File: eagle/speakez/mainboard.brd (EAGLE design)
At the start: 42 parts, among them U1 +12v

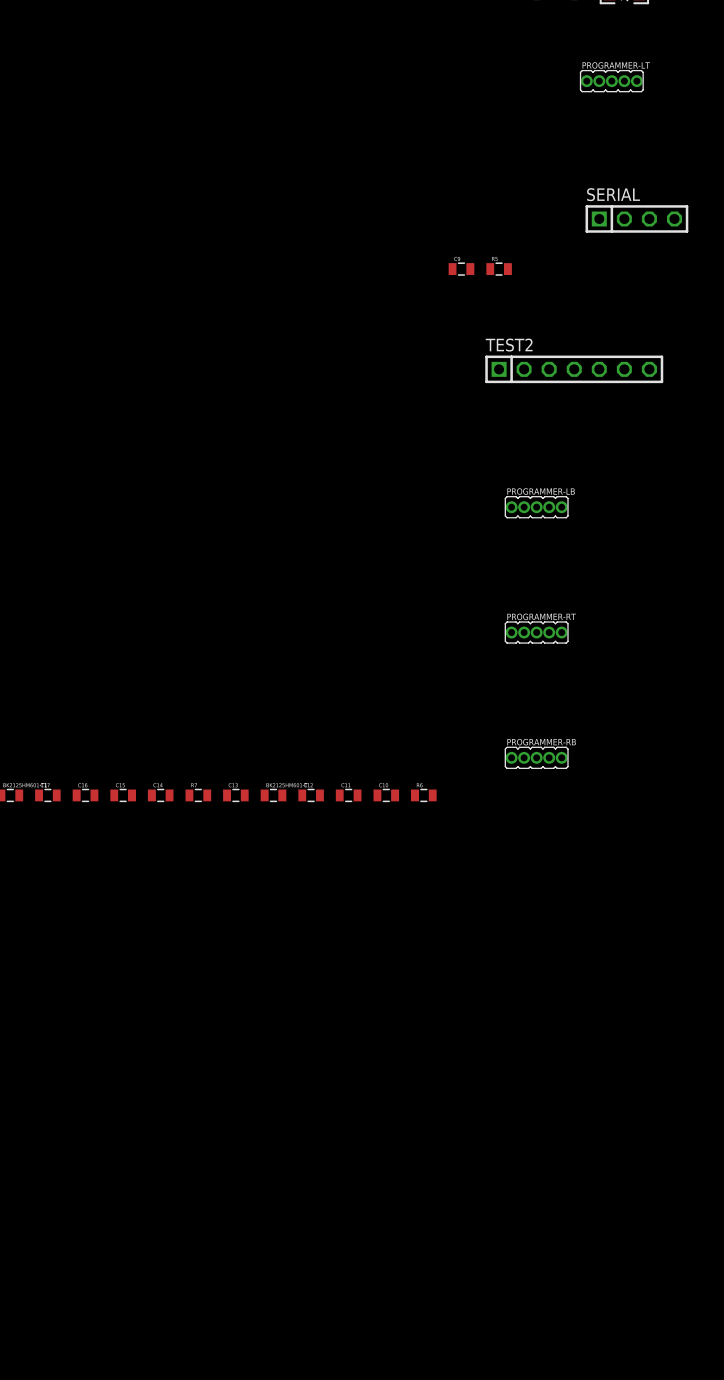
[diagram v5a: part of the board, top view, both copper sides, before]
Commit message: 0.05" header to 0.1" header
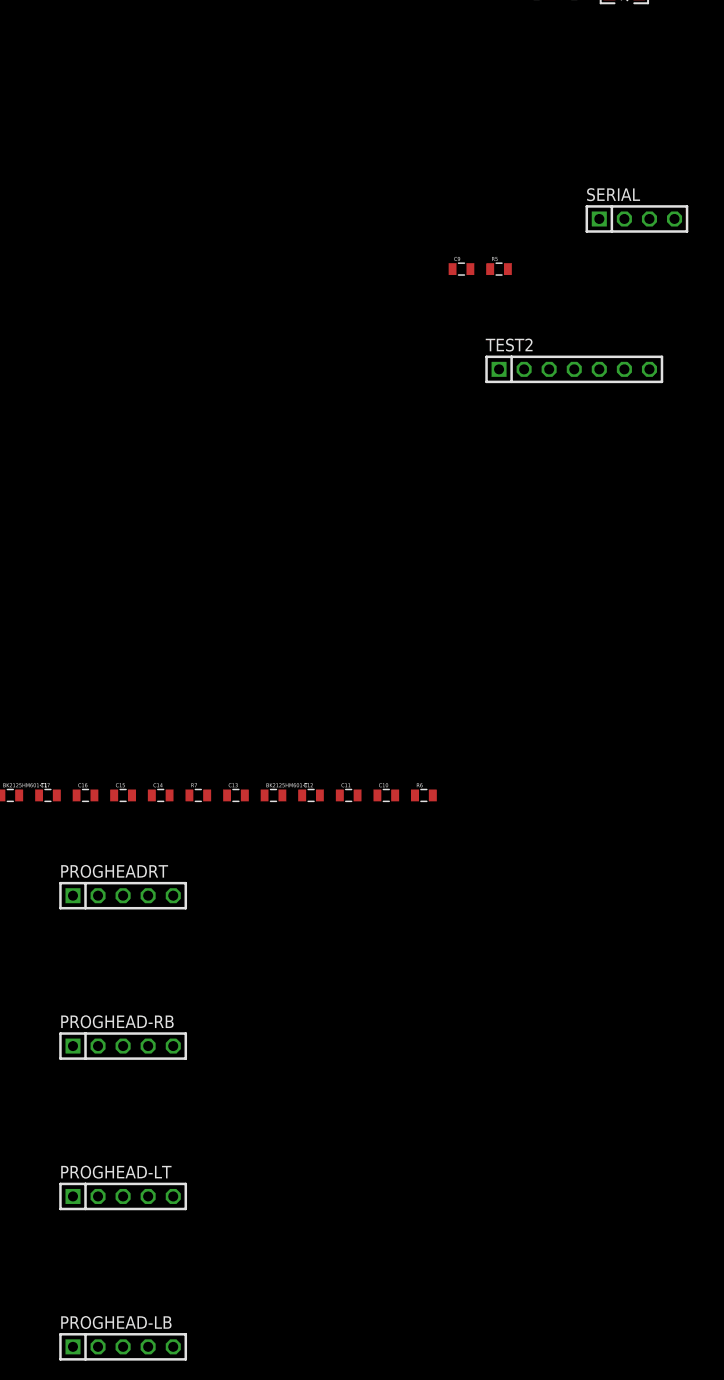
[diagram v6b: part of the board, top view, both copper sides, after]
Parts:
- removed PROGRAMMER-LB, PROGRAMMER-LT, PROGRAMMER-RB, PROGRAMMER-RT: PH1X5-05, pel_hdr:PH005-1-5
- added PROGHEAD-LB, PROGHEAD-LT, PROGHEAD-RB, PROGHEADRT: (no value), pinhead:1X05
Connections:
- net GND: now also PROGHEAD-RB.1, PROGHEAD-RB.2, PROGHEAD-RB.3, PROGHEAD-RB.4, PROGHEAD-RB.5, PROGHEADRT.2, PROGHEADRT.3, PROGHEADRT.4, PROGHEADRT.5; no longer PROGRAMMER-RB.1, PROGRAMMER-RB.2, PROGRAMMER-RB.3, PROGRAMMER-RB.4, PROGRAMMER-RB.5, PROGRAMMER-RT.2, PROGRAMMER-RT.3, PROGRAMMER-RT.4, PROGRAMMER-RT.5
- net N$14: now also PROGHEAD-LT.5; no longer PROGRAMMER-LT.5
- net N$20: now also PROGHEAD-LB.3; no longer PROGRAMMER-LB.3
- net N$21: now also PROGHEAD-LB.4; no longer PROGRAMMER-LB.4
- net N$23: now also PROGHEAD-LT.3; no longer PROGRAMMER-LT.3
- net N$24: now also PROGHEAD-LT.4; no longer PROGRAMMER-LT.4
- net N$3: now also PROGHEAD-LT.1; no longer PROGRAMMER-LT.1
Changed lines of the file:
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@@
 <element name="R3" library="SparkFun-Passives" package="0805" value="66 ohms" x="-57.15" y="-86.36"/>
 <element name="R4" library="SparkFun-Passives" package="0805" value="10k" x="-60.96" y="-86.36"/>
-<element name="PROGRAMMER-LT" library="pel_hdr" package="PH005-1-5" value="PH1X5-05" x="-55.88" y="-95.25"/>
 <element name="SERIAL" library="pinhead" package="1X04" value="" x="-50.8" y="-109.22"/>
 <element name="R5" library="SparkFun-Passives" package="0805" value="50k" x="-64.77" y="-114.3"/>
 <element name="C9" library="SparkFun-Capacitors" package="0805" value="" x="-68.58" y="-114.3"/>
 <element name="TEST2" library="pinhead" package="1X07" value="" x="-57.15" y="-124.46"/>
-<element name="PROGRAMMER-LB" library="pel_hdr" package="PH005-1-5" value="PH1X5-05" x="-63.5" y="-138.43"/>
-<element name="PROGRAMMER-RT" library="pel_hdr" package="PH005-1-5" value="PH1X5-05" x="-63.5" y="-151.13"/>
-<element name="PROGRAMMER-RB" library="pel_hdr" package="PH005-1-5" value="PH1X5-05" x="-63.5" y="-163.83"/>
 <element name="R6" library="SparkFun-Passives" package="0805" value="100k" x="-72.39" y="-167.64"/>
 <element name="C10" library="SparkFun-Capacitors" package="0805" value="0.1uF" x="-76.2" y="-167.64"/>
@@
 <element name="C17" library="SparkFun-Capacitors" package="0805" value="2.2uF" x="-110.49" y="-167.64"/>
 <element name="BK2125HM601-T1" library="SparkFun-Passives" package="0805" value="" x="-114.3" y="-167.64"/>
+<element name="PROGHEADRT" library="pinhead" package="1X05" value="" x="-102.87" y="-177.8"/>
+<element name="PROGHEAD-RB" library="pinhead" package="1X05" value="" x="-102.87" y="-193.04"/>
+<element name="PROGHEAD-LT" library="pinhead" package="1X05" value="" x="-102.87" y="-208.28"/>
+<element name="PROGHEAD-LB" library="pinhead" package="1X05" value="" x="-102.87" y="-223.52"/>
 </elements>
 <signals>
@@
 <contactref element="C11" pad="2"/>
 <contactref element="C12" pad="2"/>
-<contactref element="PROGRAMMER-RT" pad="2"/>
-<contactref element="PROGRAMMER-RT" pad="3"/>
-<contactref element="PROGRAMMER-RT" pad="4"/>
-<contactref element="PROGRAMMER-RT" pad="5"/>
-<contactref element="PROGRAMMER-RB" pad="1"/>
-<contactref element="PROGRAMMER-RB" pad="2"/>
-<contactref element="PROGRAMMER-RB" pad="3"/>
-<contactref element="PROGRAMMER-RB" pad="4"/>
-<contactref element="PROGRAMMER-RB" pad="5"/>
 <contactref element="BATTERY" pad="2"/>
 <contactref element="U1" pad="3"/>
@@
 <contactref element="C13" pad="2"/>
 <contactref element="BK2125HM601-T1" pad="2"/>
+<contactref element="PROGHEADRT" pad="2"/>
+<contactref element="PROGHEADRT" pad="3"/>
+<contactref element="PROGHEADRT" pad="4"/>
+<contactref element="PROGHEADRT" pad="5"/>
+<contactref element="PROGHEAD-RB" pad="1"/>
+<contactref element="PROGHEAD-RB" pad="2"/>
+<contactref element="PROGHEAD-RB" pad="3"/>
+<contactref element="PROGHEAD-RB" pad="4"/>
+<contactref element="PROGHEAD-RB" pad="5"/>
 <wire x1="-79.11" y1="-167.64" x2="-82.92" y2="-167.64" width="0" layer="19" extent="1-1"/>
 <wire x1="-75.3" y1="-167.64" x2="-79.11" y2="-167.64" width="0" layer="19" extent="1-1"/>
 <wire x1="-90.54" y1="-167.64" x2="-82.92" y2="-167.64" width="0" layer="19" extent="1-1"/>
 <wire x1="-98.16" y1="-167.64" x2="-90.54" y2="-167.64" width="0" layer="19" extent="1-1"/>
-<wire x1="-63.5" y1="-163.83" x2="-75.3" y2="-167.64" width="0" layer="19" extent="1-1"/>
-<wire x1="-62.23" y1="-163.83" x2="-63.5" y2="-163.83" width="0" layer="19" extent="1-1"/>
-<wire x1="-60.96" y1="-163.83" x2="-62.23" y2="-163.83" width="0" layer="19" extent="1-1"/>
-<wire x1="-59.69" y1="-163.83" x2="-60.96" y2="-163.83" width="0" layer="19" extent="1-1"/>
-<wire x1="-58.42" y1="-163.83" x2="-59.69" y2="-163.83" width="0" layer="19" extent="1-1"/>
-<wire x1="-62.23" y1="-151.13" x2="-62.23" y2="-163.83" width="0" layer="19" extent="1-1"/>
-<wire x1="-60.96" y1="-151.13" x2="-62.23" y2="-151.13" width="0" layer="19" extent="1-1"/>
-<wire x1="-59.69" y1="-151.13" x2="-60.96" y2="-151.13" width="0" layer="19" extent="1-1"/>
-<wire x1="-58.42" y1="-151.13" x2="-59.69" y2="-151.13" width="0" layer="19" extent="1-1"/>
-<wire x1="-113.4" y1="-167.64" x2="-98.16" y2="-167.64" width="0" layer="19" extent="1-1"/>
-<wire x1="-65.67" y1="-114.3" x2="-62.23" y2="-151.13" width="0" layer="19" extent="1-1"/>
+<wire x1="-97.79" y1="-177.8" x2="-98.16" y2="-167.64" width="0" layer="19" extent="1-1"/>
+<wire x1="-100.33" y1="-177.8" x2="-97.79" y2="-177.8" width="0" layer="19" extent="1-1"/>
+<wire x1="-102.87" y1="-177.8" x2="-100.33" y2="-177.8" width="0" layer="19" extent="1-1"/>
+<wire x1="-105.41" y1="-177.8" x2="-102.87" y2="-177.8" width="0" layer="19" extent="1-1"/>
+<wire x1="-113.4" y1="-167.64" x2="-105.41" y2="-177.8" width="0" layer="19" extent="1-1"/>
+<wire x1="-105.41" y1="-193.04" x2="-105.41" y2="-177.8" width="0" layer="19" extent="1-1"/>
+<wire x1="-107.95" y1="-193.04" x2="-105.41" y2="-193.04" width="0" layer="19" extent="1-1"/>
+<wire x1="-102.87" y1="-193.04" x2="-105.41" y2="-193.04" width="0" layer="19" extent="1-1"/>
+<wire x1="-100.33" y1="-193.04" x2="-102.87" y2="-193.04" width="0" layer="19" extent="1-1"/>
+<wire x1="-97.79" y1="-193.04" x2="-100.33" y2="-193.04" width="0" layer="19" extent="1-1"/>
+<wire x1="-65.67" y1="-114.3" x2="-75.3" y2="-167.64" width="0" layer="19" extent="1-1"/>
 <wire x1="-46.99" y1="-109.22" x2="-65.67" y2="-114.3" width="0" layer="19" extent="1-1"/>
 <wire x1="-58.05" y1="-86.36" x2="-46.99" y2="-109.22" width="0" layer="19" extent="1-1"/>
@@
 <contactref element="SERIAL" pad="3"/>
 <contactref element="TEST2" pad="1"/>
-<contactref element="PROGRAMMER-LT" pad="1"/>
 <contactref element="R6" pad="1"/>
 <contactref element="C10" pad="1"/>
@@
 <contactref element="TEST2" pad="6"/>
 <contactref element="TEST2" pad="7"/>
+<contactref element="PROGHEAD-LT" pad="1"/>
 <wire x1="-80.91" y1="-167.64" x2="-84.72" y2="-167.64" width="0" layer="19" extent="1-1"/>
 <wire x1="-77.1" y1="-167.64" x2="-80.91" y2="-167.64" width="0" layer="19" extent="1-1"/>
@@
 <wire x1="-92.34" y1="-167.64" x2="-88.53" y2="-167.64" width="0" layer="19" extent="1-1"/>
 <wire x1="-99.96" y1="-167.64" x2="-92.34" y2="-167.64" width="0" layer="19" extent="1-1"/>
+<wire x1="-107.95" y1="-208.28" x2="-99.96" y2="-167.64" width="0" layer="19" extent="1-1"/>
 <wire x1="-64.77" y1="-124.46" x2="-73.29" y2="-167.64" width="0" layer="19" extent="1-1"/>
 <wire x1="-52.07" y1="-124.46" x2="-64.77" y2="-124.46" width="0" layer="19" extent="1-1"/>
 <wire x1="-49.53" y1="-124.46" x2="-52.07" y2="-124.46" width="0" layer="19" extent="1-1"/>
 <wire x1="-49.53" y1="-109.22" x2="-49.53" y2="-124.46" width="0" layer="19" extent="1-1"/>
-<wire x1="-55.88" y1="-95.25" x2="-49.53" y2="-109.22" width="0" layer="19" extent="1-1"/>
-<wire x1="-61.86" y1="-86.36" x2="-55.88" y2="-95.25" width="0" layer="19" extent="1-1"/>
+<wire x1="-61.86" y1="-86.36" x2="-49.53" y2="-109.22" width="0" layer="19" extent="1-1"/>
 <wire x1="-54.24" y1="-81.28" x2="-61.86" y2="-86.36" width="0" layer="19" extent="1-1"/>
 <wire x1="-46.62" y1="-81.28" x2="-54.24" y2="-81.28" width="0" layer="19" extent="1-1"/>
@@
 <contactref element="R4" pad="2"/>
 <contactref element="TEST2" pad="2"/>
-<contactref element="PROGRAMMER-LB" pad="3"/>
-<wire x1="-62.23" y1="-124.46" x2="-60.96" y2="-138.43" width="0" layer="19" extent="1-1"/>
+<contactref element="PROGHEAD-LB" pad="3"/>
 <wire x1="-60.06" y1="-86.36" x2="-62.23" y2="-124.46" width="0" layer="19" extent="1-1"/>
 <wire x1="-14.605" y1="-18.4912" x2="-60.06" y2="-86.36" width="0" layer="19" extent="1-1"/>
+<wire x1="-102.87" y1="-223.52" x2="-62.23" y2="-124.46" width="0" layer="19" extent="1-1"/>
 </signal>
 <signal name="N$23">
 <contactref element="U$1" pad="24"/>
-<contactref element="PROGRAMMER-LT" pad="3"/>
-<wire x1="-20.574" y1="-20.955" x2="-53.34" y2="-95.25" width="0" layer="19" extent="1-1"/>
+<contactref element="PROGHEAD-LT" pad="3"/>
+<wire x1="-20.574" y1="-20.955" x2="-102.87" y2="-208.28" width="0" layer="19" extent="1-1"/>
 </signal>
 <signal name="N$24">
 <contactref element="U$1" pad="25"/>
-<contactref element="PROGRAMMER-LT" pad="4"/>
 <contactref element="R6" pad="2"/>
-<wire x1="-52.07" y1="-95.25" x2="-71.49" y2="-167.64" width="0" layer="19" extent="1-1"/>
-<wire x1="-20.066" y1="-20.955" x2="-52.07" y2="-95.25" width="0" layer="19" extent="1-1"/>
+<contactref element="PROGHEAD-LT" pad="4"/>
+<wire x1="-100.33" y1="-208.28" x2="-71.49" y2="-167.64" width="0" layer="19" extent="1-1"/>
+<wire x1="-20.066" y1="-20.955" x2="-71.49" y2="-167.64" width="0" layer="19" extent="1-1"/>
 </signal>
 <signal name="N$25">
@@
 <signal name="N$14">
 <contactref element="U$1" pad="22"/>
-<contactref element="PROGRAMMER-LT" pad="5"/>
-<wire x1="-21.5646" y1="-20.955" x2="-50.8" y2="-95.25" width="0" layer="19" extent="1-1"/>
+<contactref element="PROGHEAD-LT" pad="5"/>
+<wire x1="-21.5646" y1="-20.955" x2="-97.79" y2="-208.28" width="0" layer="19" extent="1-1"/>
 </signal>
 <signal name="N$21">
 <contactref element="U$1" pad="23"/>
-<contactref element="PROGRAMMER-LB" pad="4"/>
-<wire x1="-21.082" y1="-20.955" x2="-59.69" y2="-138.43" width="0" layer="19" extent="1-1"/>
+<contactref element="PROGHEAD-LB" pad="4"/>
+<wire x1="-21.082" y1="-20.955" x2="-100.33" y2="-223.52" width="0" layer="19" extent="1-1"/>
 </signal>
 <signal name="N$29">

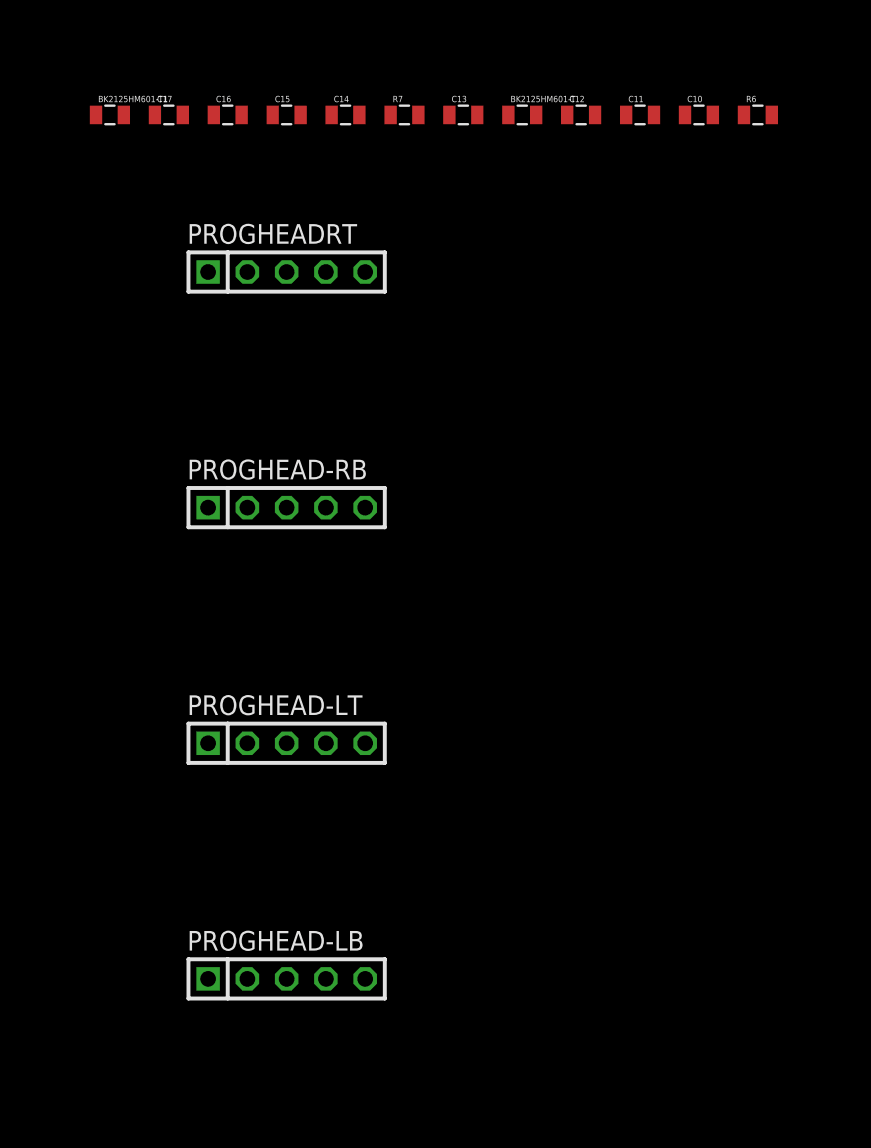
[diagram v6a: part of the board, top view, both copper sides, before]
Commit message: update jlink connector
also add jtag support
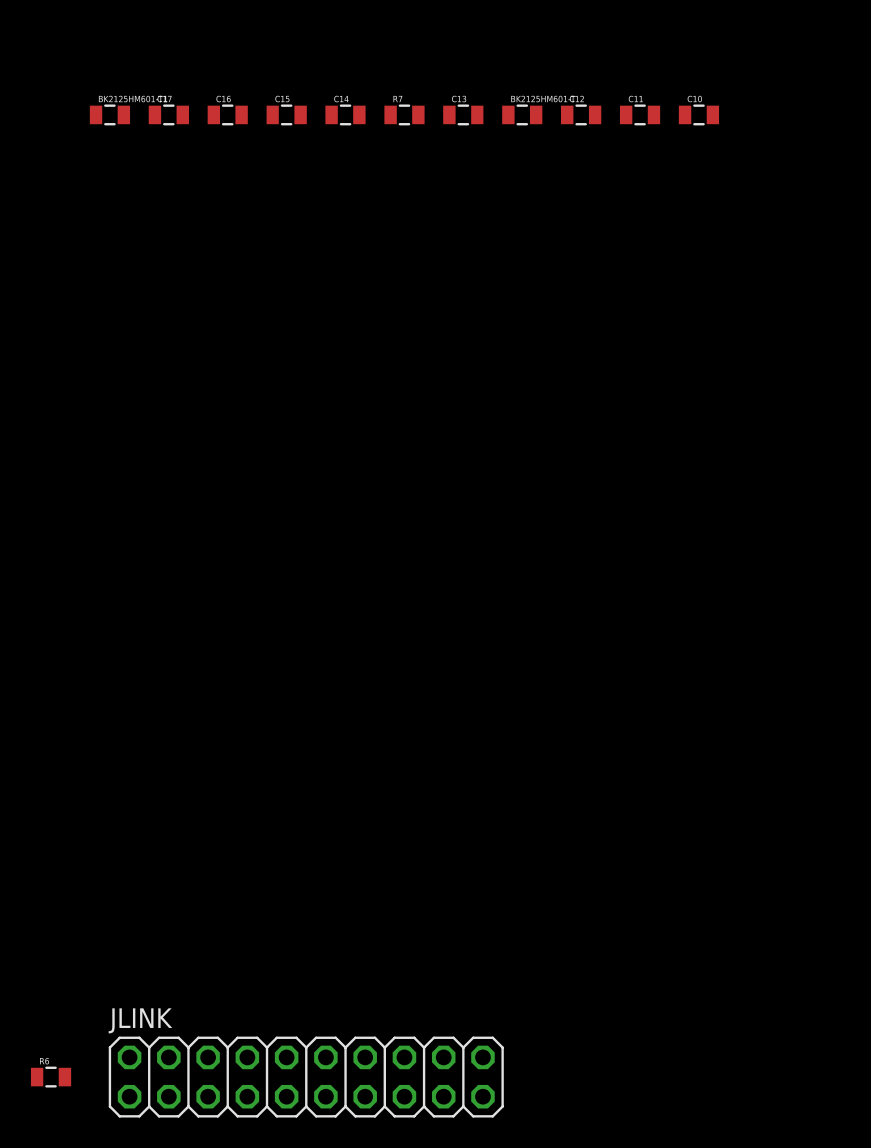
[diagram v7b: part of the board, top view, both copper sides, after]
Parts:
- removed PROGHEAD-LB, PROGHEAD-LT, PROGHEAD-RB, PROGHEADRT: (no value), pinhead:1X05
- added JLINK: JLINK, pinhead:2X10
- moved R6 77.2 mm to (-118.1, -229.9)
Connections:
- removed net N$20: PROGHEAD-LB.3, R4.2, TEST2.2, U$1.34
- removed net N$21: PROGHEAD-LB.4, U$1.23
- new net +5V: BATTERY.1, D1.A, JLINK.19
- new net N$16: JLINK.3, U$1.27
- new net RESET: JLINK.15, R4.2, TEST2.2, U$1.34
- net GND: no longer PROGHEAD-RB.1, PROGHEAD-RB.2, PROGHEAD-RB.3, PROGHEAD-RB.4, PROGHEAD-RB.5, PROGHEADRT.2, PROGHEADRT.3, PROGHEADRT.4, PROGHEADRT.5
- net N$13: now also JLINK.5, U$1.23; no longer BATTERY.1, D1.A
- net N$14: now also JLINK.9; no longer PROGHEAD-LT.5
- net N$23: now also JLINK.13, JLINK.17; no longer PROGHEAD-LT.3
- net N$24: now also JLINK.7; no longer PROGHEAD-LT.4
- net N$29: now also JLINK.10, JLINK.12, JLINK.14, JLINK.16, JLINK.18, JLINK.20, JLINK.4, JLINK.6, JLINK.8
- net N$3: now also JLINK.1; no longer PROGHEAD-LT.1

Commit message: started moving things around
oh god so many passives
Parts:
- moved R6 313.9 mm to (43.2, 39.4)
- moved C17 275.2 mm to (73.7, 36.8)
- moved C14 270.8 mm to (80.0, 35.6)
- moved C11 264.7 mm to (80.0, 43.2)
- moved BK2125HM601-T1 264.2 mm to (54.6, 35.6)
- moved C12 264.0 mm to (80.0, 39.4)
- moved JLINK 261.8 mm to (14.0, 5.08)
- moved C16 256.5 mm to (54.6, 31.8)
- moved C13 249.2 mm to (59.7, 30.5)
- moved C15 245.9 mm to (44.5, 29.2)
- moved R7 238.3 mm to (44.5, 25.4)
- moved C10 228.4 mm to (20.3, 39.4)
- moved BK2125HM601-T 227.2 mm to (38.1, 21.6)
- moved R5 197.0 mm to (66.0, 33.0)
- moved C9 197.0 mm to (54.6, 39.4)
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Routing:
- net N$11: track 158.0 -> 234.2 mm
- net N$12: track 66.0 -> 45.7 mm
